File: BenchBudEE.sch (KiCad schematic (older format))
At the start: 0 parts

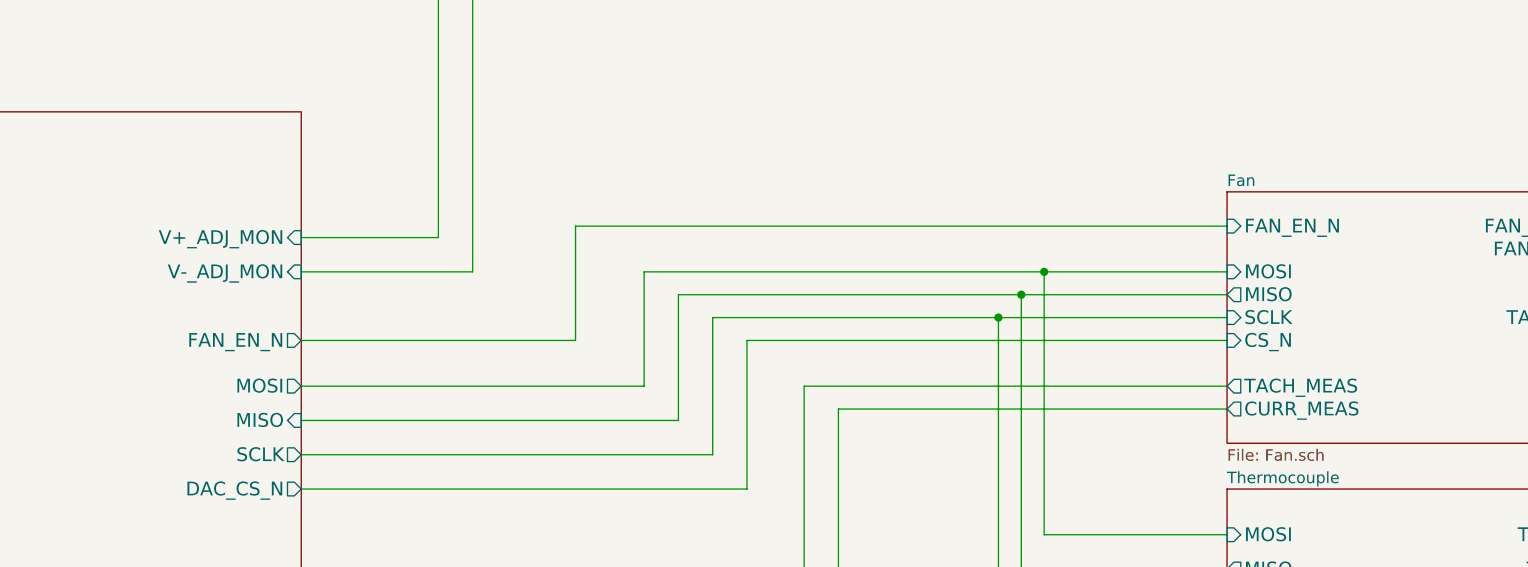
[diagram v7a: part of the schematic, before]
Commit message: Module 3, Unit 10: Revisiting The Current/Fan Module
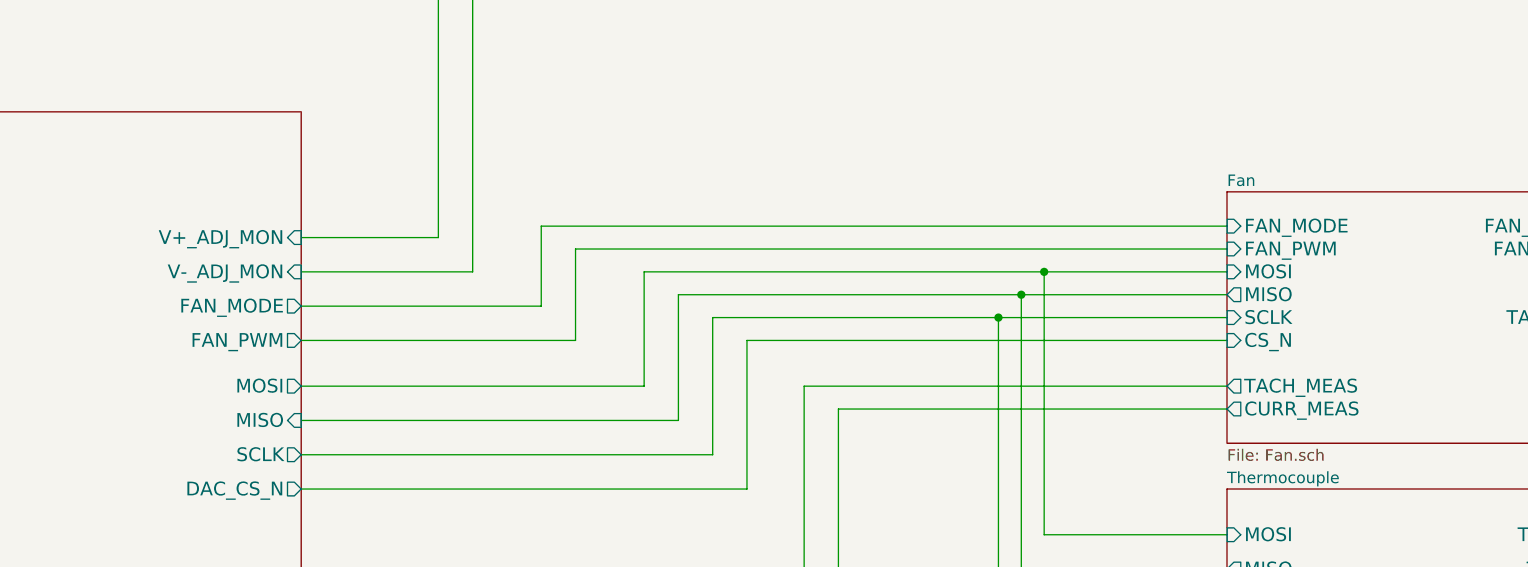
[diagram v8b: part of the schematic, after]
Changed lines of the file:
@@
 F7 "TACH_IN" I R 9550 3600 60
 F8 "TACH_MEAS" O L 7900 3900 60
-F9 "FAN_EN_N" I L 7900 3200 60
-F10 "CURR_MEAS" O L 7900 4000 60
-F11 "FAN_OUT-" O R 9550 3300 60
+F9 "CURR_MEAS" O L 7900 4000 60
+F10 "FAN_OUT-" O R 9550 3300 60
+F11 "FAN_PWM" I L 7900 3300 60
+F12 "FAN_MODE" I L 7900 3200 60
 $EndSheet
 $Sheet
@@
 Wire Wire Line
 	3850 3700 5050 3700
-Wire Wire Line
-	5050 3700 5050 3200
-Wire Wire Line
-	5050 3200 7900 3200
 Wire Wire Line
 	3850 3900 5350 3900
@@
 F6 "RELAY+" O R 3850 6050 60
 F7 "RELAY-" I R 3850 6200 60
-F8 "FAN_EN_N" O R 3850 3700 60
-F9 "CURR_MEAS" I R 3850 5000 60
-F10 "V+_ADJ_MON" I R 3850 3250 60
-F11 "V-_ADJ_MON" I R 3850 3400 60
-F12 "LED_EN_PWM" O R 3850 5600 60
-F13 "DAC_CS_N" O R 3850 4350 60
-F14 "ADC_CS_N" O R 3850 5250 60
+F8 "CURR_MEAS" I R 3850 5000 60
+F9 "V+_ADJ_MON" I R 3850 3250 60
+F10 "V-_ADJ_MON" I R 3850 3400 60
+F11 "LED_EN_PWM" O R 3850 5600 60
+F12 "DAC_CS_N" O R 3850 4350 60
+F13 "ADC_CS_N" O R 3850 5250 60
+F14 "FAN_PWM" O R 3850 3700 60
+F15 "FAN_MODE" O R 3850 3550 60
 $EndSheet
 Wire Wire Line
@@
 Wire Wire Line
 	6750 6200 3850 6200
+Wire Wire Line
+	5050 3700 5050 3300
+Wire Wire Line
+	5050 3300 7900 3300
+Wire Wire Line
+	3850 3550 4900 3550
+Wire Wire Line
+	4900 3550 4900 3200
+Wire Wire Line
+	4900 3200 7900 3200
 $EndSCHEMATC
